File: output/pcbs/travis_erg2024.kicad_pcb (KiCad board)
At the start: 2 copper layers, 385.3 x 144.8 mm, 378 parts, among them SW1 SW_PUSH_6mm_H4.3mm

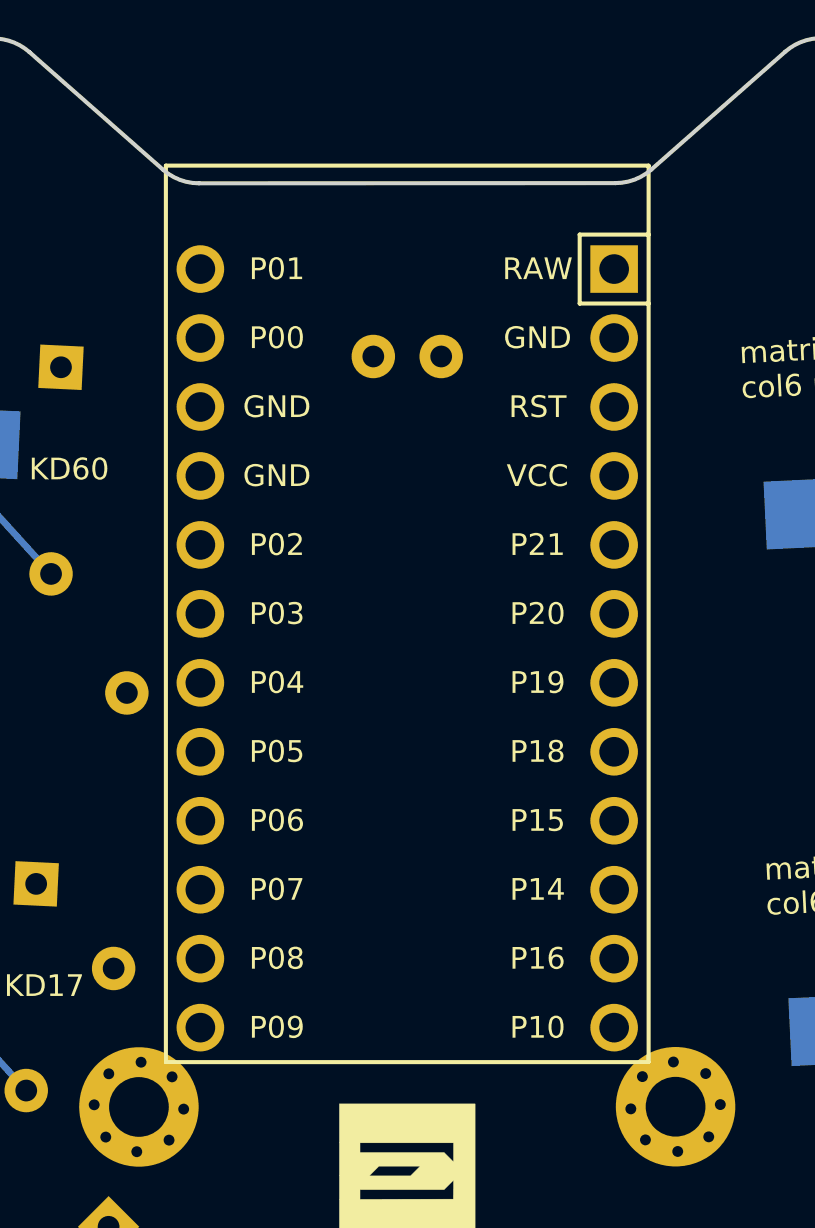
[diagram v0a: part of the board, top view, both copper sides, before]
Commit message: new mcu footprint, mux fixes
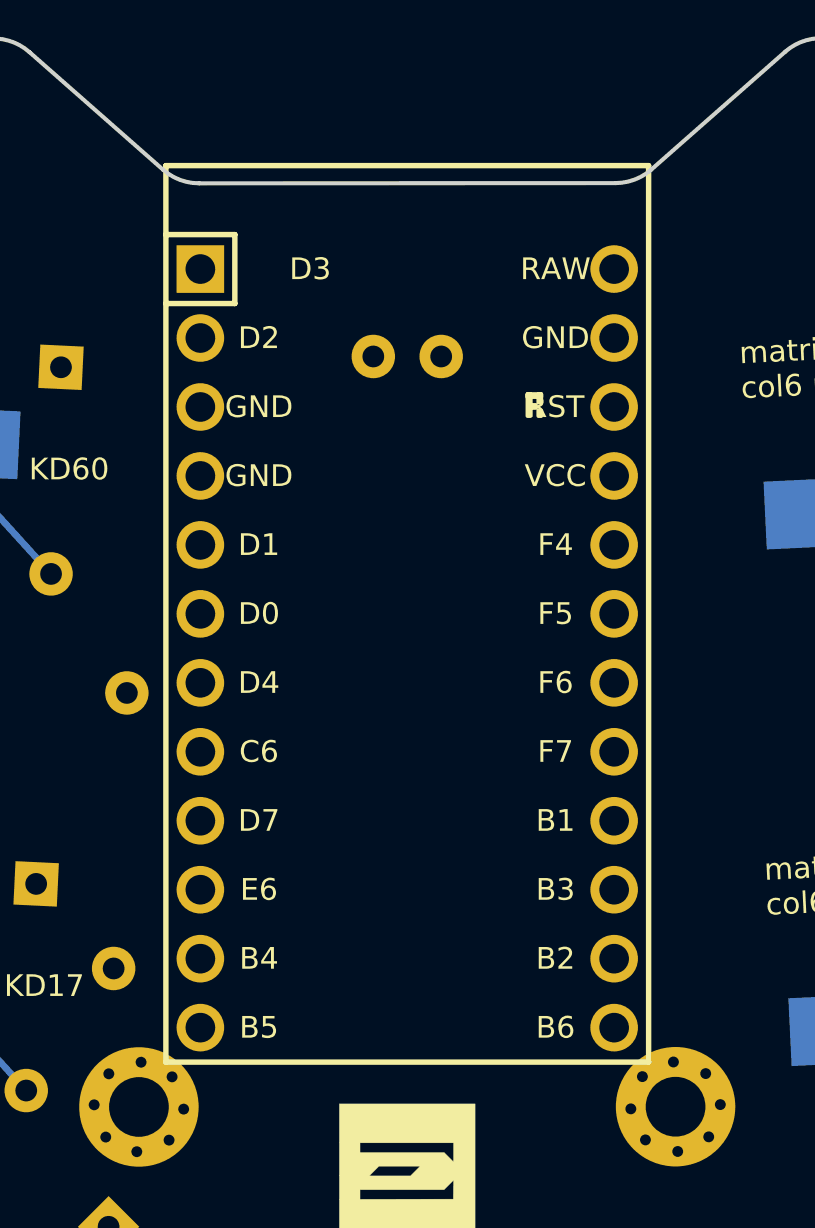
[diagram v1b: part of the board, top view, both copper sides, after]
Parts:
- DIP1, DIP2: value DIP-16_W7.62mm_Socket -> 74HC138N
- MCU1: value (none) -> Arduino_Pro_Micro; footprint ProMicro -> Arduino_Pro_Micro
- turned MCU1 to 0 degrees
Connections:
- DIP1 pad 10: col0 -> col2
- DIP1 pad 11: col1 -> col3
- DIP1 pad 12: col2 -> col4
- DIP1 pad 13: col3 -> col5
- DIP1 pad 14: col4 -> col6
- DIP1 pad 15: col5 -> col7
- DIP1 pad 7: row0 -> col0
- DIP1 pad 9: row1 -> col1
- MCU1 pad 1: RAW -> D3
- MCU1 pad 10: row5 -> scrA
- MCU1 pad 11: encA -> B4
- MCU1 pad 12: encC -> LED
- MCU1 pad 13: P1 -> encC
- MCU1 pad 14: P0 -> encA
- MCU1 pad 15: GND -> row5
- MCU1 pad 16: GND -> row4
- MCU1 pad 17: mux3 -> row3
- MCU1 pad 18: mux2 -> row2
- MCU1 pad 19: mux1 -> row1
- MCU1 pad 2: GND -> D2
- MCU1 pad 20: mux0 -> row0
- MCU1 pad 21: scrC -> VCC
- MCU1 pad 22: scrA -> RST
- MCU1 pad 23: P8 -> GND
- MCU1 pad 24: LED -> RAW
- MCU1 pad 3: RST -> GND
- MCU1 pad 4: VCC -> GND
- MCU1 pad 5: col7 -> mux3
- MCU1 pad 6: col6 -> mux2
- MCU1 pad 7: row2 -> mux1
- MCU1 pad 8: row3 -> mux0
- MCU1 pad 9: row4 -> scrC

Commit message: [200~evqwgd001~ footprint added
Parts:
- removed REF**: RollerEncoder_Panasonic_EVQWGD001, RollerEncoder_Panasonic_EVQWGD001
- added SCR1: RollerEncoder_Panasonic_EVQWGD001, travis:evqwgd001, F.Cu at (163.1, 142.0)
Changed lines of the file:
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@@
 (net 214 "RST")
 (net 215 "scr_to")
-(net 216 "undefined")
-(net 217 "enc_to")
+(net 216 "enc_to")
   (net_class Default "This is the default net class."
     (clearance 0.2)
@@
 (add_net "RST")
 (add_net "scr_to")
-(add_net "undefined")
 (add_net "enc_to")
   )
@@
         (effects (font (size 0.8 0.8) (thickness 0.15)))
     )
-    (fp_text user "D3" (at -3.571872 -13.97) (layer "F.SilkS")
+    (fp_text user "D3" (at -5.461 -13.97) (layer "F.SilkS")
         (effects (font (size 0.8 0.8) (thickness 0.15)))
     )
-    (fp_text user "D3" (at -3.571872 -13.97) (layer "B.SilkS")
+    (fp_text user "D3" (at -5.461 -13.97) (layer "B.SilkS")
         (effects (font (size 0.8 0.8) (thickness 0.15)) (justify mirror))
     )
@@
     )
   )
-        (module RollerEncoder_Panasonic_EVQWGD001 (layer F.Cu)
+        (module "travis:evqwgd001" (layer F.Cu)
         (at 163.14529764999997 141.96773245 0)
-        (fp_text reference REF** (at 0 0 0) (layer F.Fab) (effects (font (size 1 1) (thickness 0.15))))
-        (fp_text value RollerEncoder_Panasonic_EVQWGD001 (at -0.1 9 0) (layer F.Fab) (effects (font (size 1 1) (thickness 0.15))))
+        (attr through_hole)
+        (fp_text reference "SCR1" (at 0 0 0) (layer F.SilkS) hide
+            (effects (font (size 1 1) (thickness 0.15)))
+        )
+        (fp_text value "RollerEncoder_Panasonic_EVQWGD001" (at -0.1 9 0) (layer F.Fab) hide
+            (effects (font (size 0.8 0.8) (thickness 0.15)))
+        )
         (fp_line (start -8.4 -6.4) (end 8.4 -6.4) (layer Dwgs.User) (width 0.12))
         (fp_line (start 8.4 -6.4) (end 8.4 7.4) (layer Dwgs.User) (width 0.12))
@@
           (pad B thru_hole circle (at -5.625 -1.27 0) (size 1.6 1.6) (drill 0.9) (layers *.Cu *.Mask) (net 7 "GND"))
           (pad C thru_hole circle (at -5.625 1.27 0) (size 1.6 1.6) (drill 0.9) (layers *.Cu *.Mask) (net 208 "scrC"))
-          (pad D thru_hole circle (at -5.625 3.81 0) (size 1.6 1.6) (drill 0.9) (layers *.Cu *.Mask) (net 216 "undefined"))
+          (pad D thru_hole circle (at -5.625 3.81 0) (size 1.6 1.6) (drill 0.9) (layers *.Cu *.Mask) (net 0 ""))
           (pad "" np_thru_hole circle (at -5.625 6.3 0) (size 1.5 1.5) (drill 1.5) (layers *.Cu *.Mask))
-        )
+        (model "${TRAVIS_KICAD}/evqwgd001.step"
+    (offset (xyz 8.5 -7.4 -3.5))
+    (scale (xyz 1 1 1))
+    (rotate (xyz 0 0 -90))
+  )
+)
     (module "ScottoKeebs_Components:Diode_DO-35" (layer "B.Cu")
     (descr "Diode, DO-35_SOD27 series, Axial, Horizontal, pin pitch=7.62mm, , length*diameter=4*2mm^2, , http://www.diodes.com/_files/packages/DO-35.pdf")
@@
             (pad B thru_hole circle (at -7.62 2.46) (size 2 2) (drill 1) (layers *.Cu *.Mask) (net 7 "GND"))
             (pad 1 thru_hole circle (at 6.88 -2.54) (size 1.5 1.5) (drill 1) (layers *.Cu *.Mask) (net 38 "col4"))
-            (pad 2 thru_hole circle (at 6.88 2.46) (size 1.5 1.5) (drill 1) (layers *.Cu *.Mask) (net 217 "enc_to"))
+            (pad 2 thru_hole circle (at 6.88 2.46) (size 1.5 1.5) (drill 1) (layers *.Cu *.Mask) (net 216 "enc_to"))
             (pad "" thru_hole rect (at -0.12 -5.64 -90) (size 3.2 2) (drill oval 2.8 1.5) (layers *.Cu *.Mask))
             (pad "" thru_hole rect (at -0.12 5.56 -90)  (size 3.2 2) (drill oval 2.8 1.5) (layers *.Cu *.Mask))
@@
       (stroke (width 0.1) (type solid)) (layer "B.Fab") )
     (pad 1 thru_hole rect (at 0 0 45) (size 1.6 1.6) (drill 0.8) (layers "*.Cu" "*.Mask") (net 3 "row5"))
-    (pad 2 thru_hole oval (at 7.62 0 45) (size 1.6 1.6) (drill 0.8) (layers "*.Cu" "*.Mask") (net 217 "enc_to"))
+    (pad 2 thru_hole oval (at 7.62 0 45) (size 1.6 1.6) (drill 0.8) (layers "*.Cu" "*.Mask") (net 216 "enc_to"))
     (model "${SCOTTOKEEBS_KICAD}/3dmodels/ScottoKeebs_Components.3dshapes/Diode_DO-35.step"
       (offset (xyz 0 0 0))

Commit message: added ec11
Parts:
- ROT1: value (none) -> EC11; footprint rotary_encoder -> travis:ec11
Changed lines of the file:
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@@
     )
   )
-        (module rotary_encoder (layer F.Cu)
+        (module "travis:ec11" (layer F.Cu)
             (at 163.145297625 170.50982505000002 -90)
-            (fp_text reference "ROT1" (at 0 0.5) (layer F.SilkS)
-                hide (effects (font (size 1 1) (thickness 0.15))))
-            (fp_text value "" (at 0 8.89) (layer F.Fab)
-                (effects (font (size 1 1) (thickness 0.15))))
+            (fp_text reference "ROT1" (at 0 0.5 -90) (layer F.SilkS) hide
+                (effects (font (size 1 1) (thickness 0.15)))
+            )
+            (fp_text value "EC11" (at 0 8.89 -90) (layer F.Fab) hide
+                (effects (font (size 0.8 0.8) (thickness 0.15)))
+            )
             (fp_line (start -0.62 -0.04) (end 0.38 -0.04) (layer F.SilkS) (width 0.12))
             (fp_line (start -0.12 -0.54) (end -0.12 0.46) (layer F.SilkS) (width 0.12))
@@
             (pad "" thru_hole rect (at -0.12 -5.64 -90) (size 3.2 2) (drill oval 2.8 1.5) (layers *.Cu *.Mask))
             (pad "" thru_hole rect (at -0.12 5.56 -90)  (size 3.2 2) (drill oval 2.8 1.5) (layers *.Cu *.Mask))
+            (model "${TRAVIS_KICAD}/ec11.step"
+                (offset (xyz 0 0 0))
+                (scale (xyz 1 1 1))
+                (rotate (xyz 0 0 90))
+            )
         )
     (module "ScottoKeebs_Components:Diode_DO-35" (layer "B.Cu")

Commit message: wired v5
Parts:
- moved D1 5.30 mm to (157.1, 126.2), turned to -90 degrees
- moved D2 5.00 mm to (158.6, 185.0), turned to 90 degrees
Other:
- board text added: "2024.03.31"
- board text removed: "2024.03.25"
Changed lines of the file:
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@@
   (title_block
     (title travis_erg2024)
-    (rev 2024.03.25)
+    (rev 2024.03.31)
     (company "Travis Hardiman")
   )
@@
     (descr "Diode, DO-35_SOD27 series, Axial, Horizontal, pin pitch=7.62mm, , length*diameter=4*2mm^2, , http://www.diodes.com/_files/packages/DO-35.pdf")
     (tags "Diode DO-35_SOD27 series Axial Horizontal pin pitch 7.62mm  length 4mm diameter 2mm")
-    (at 152.14529764999997 127.96773245 -45)
-    (fp_text reference "D1" (at 3.81 -2.12 -45) (layer "B.SilkS") hide
+    (at 157.14529764999997 126.21773245 -90)
+    (fp_text reference "D1" (at 3.81 -2.12 -90) (layer "B.SilkS") hide
       (effects (font (size 1 1) (thickness 0.15)) (justify mirror))
     )
-    (fp_text value "1N4148" (at 3.81 0 -45) (layer "B.Fab")
+    (fp_text value "1N4148" (at 3.81 0 -90) (layer "B.Fab")
       (effects (font (size 0.8 0.8) (thickness 0.15)))
     )
@@
     (fp_line (start 7.62 0) (end 5.81 0)
       (stroke (width 0.1) (type solid)) (layer "B.Fab") )
-    (pad 1 thru_hole rect (at 0 0 -45) (size 1.6 1.6) (drill 0.8) (layers "*.Cu" "*.Mask") (net 122 "row0"))
-    (pad 2 thru_hole oval (at 7.62 0 -45) (size 1.6 1.6) (drill 0.8) (layers "*.Cu" "*.Mask") (net 215 "scr_to"))
+    (pad 1 thru_hole rect (at 0 0 -90) (size 1.6 1.6) (drill 0.8) (layers "*.Cu" "*.Mask") (net 122 "row0"))
+    (pad 2 thru_hole oval (at 7.62 0 -90) (size 1.6 1.6) (drill 0.8) (layers "*.Cu" "*.Mask") (net 215 "scr_to"))
     (model "${SCOTTOKEEBS_KICAD}/3dmodels/ScottoKeebs_Components.3dshapes/Diode_DO-35.step"
       (offset (xyz 0 0 0))
@@
     (descr "Diode, DO-35_SOD27 series, Axial, Horizontal, pin pitch=7.62mm, , length*diameter=4*2mm^2, , http://www.diodes.com/_files/packages/DO-35.pdf")
     (tags "Diode DO-35_SOD27 series Axial Horizontal pin pitch 7.62mm  length 4mm diameter 2mm")
-    (at 153.645297625 185.00982505000002 45)
-    (fp_text reference "D2" (at 3.81 -2.12 -45) (layer "B.SilkS") hide
+    (at 158.645297625 185.00982505000002 90)
+    (fp_text reference "D2" (at 3.81 -2.12 -90) (layer "B.SilkS") hide
       (effects (font (size 1 1) (thickness 0.15)) (justify mirror))
     )
-    (fp_text value "1N4148" (at 3.81 0 -45) (layer "B.Fab")
+    (fp_text value "1N4148" (at 3.81 0 -90) (layer "B.Fab")
       (effects (font (size 0.8 0.8) (thickness 0.15)))
     )
@@
     (fp_line (start 7.62 0) (end 5.81 0)
       (stroke (width 0.1) (type solid)) (layer "B.Fab") )
-    (pad 1 thru_hole rect (at 0 0 45) (size 1.6 1.6) (drill 0.8) (layers "*.Cu" "*.Mask") (net 3 "row5"))
-    (pad 2 thru_hole oval (at 7.62 0 45) (size 1.6 1.6) (drill 0.8) (layers "*.Cu" "*.Mask") (net 216 "enc_to"))
+    (pad 1 thru_hole rect (at 0 0 90) (size 1.6 1.6) (drill 0.8) (layers "*.Cu" "*.Mask") (net 3 "row5"))
+    (pad 2 thru_hole oval (at 7.62 0 90) (size 1.6 1.6) (drill 0.8) (layers "*.Cu" "*.Mask") (net 216 "enc_to"))
     (model "${SCOTTOKEEBS_KICAD}/3dmodels/ScottoKeebs_Components.3dshapes/Diode_DO-35.step"
       (offset (xyz 0 0 0))
@@
        (stroke (width 0) (type solid)) (fill solid) (layer F.Cu))
    )
-      (gr_text "2024.03.25" (at 163.14529770000001 200.22995045 0) (layer F.SilkS)
+      (gr_text "2024.03.31" (at 163.14529770000001 200.22995045 0) (layer F.SilkS)
         (effects (font (face "CaskaydiaMono NFP") (size 0.9 0.9) (thickness 0.15)))
       )

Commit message: minor value updates
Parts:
- C1: value C_Radial_D6.3mm_H11.0mm_P2.50mm -> 6.3V 1000uF
- C2, C3: value C_Disc_D3.8mm_W2.6mm_P2.50mm -> 104
- KLED1, KLED10, KLED11, KLED12, KLED13, KLED14, KLED15, KLED16, KLED17, KLED18, KLED19, KLED2, KLED20, KLED21, KLED22, KLED23, KLED24, KLED25, KLED26, KLED27, KLED28, KLED29, KLED3, KLED30, KLED31, KLED32, KLED33, KLED34, KLED35, KLED36, KLED37, KLED38, KLED39, KLED4, KLED40, KLED41, KLED42, KLED43, KLED44, KLED45, KLED46, KLED47, KLED48, KLED49, KLED5, KLED50, KLED51, KLED52, KLED53, KLED54, KLED55, KLED56, KLED57, KLED58, KLED59, KLED6, KLED60, KLED61, KLED62, KLED63, KLED64, KLED65, KLED66, KLED67, KLED68, KLED69, KLED7, KLED70, KLED71, KLED72, KLED73, KLED74, KLED75, KLED76, KLED77, KLED78, KLED79, KLED8, KLED80, KLED81, KLED82, KLED83, KLED84, KLED85, KLED86, KLED87, KLED88, KLED9: footprint travis:led_SK6812mini-e (per-key single-side) -> travis:led_SK6812mini-e
- MCU1: value Arduino_Pro_Micro -> Arduino Pro Micro
- R1: value R_Axial_DIN0207_L6.3mm_D2.5mm_P10.16mm_Horizontal -> 470R
- SCR1: value RollerEncoder_Panasonic_EVQWGD001 -> EVQWGD001
- SW1: value SW_PUSH_6mm_H4.3mm -> 6mm button
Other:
- board text added: "2024.04.01"
- board text removed: "2024.03.31"

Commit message: v6 of routing
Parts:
- C2, C3: footprint Capacitor_THT:C_Disc_D3.8mm_W2.6mm_P2.50mm -> Capacitor_THT:C_Disc_D4.7mm_W2.5mm_P5.00mm
- DIP1, DIP2: value 74HC138N -> SN74HC138N
- moved C3 1.27 mm to (267.5, 87.9)
- moved C2 1.27 mm to (63.3, 89.1)
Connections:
- DIP1 pad 10: col2 -> col5
- DIP1 pad 11: col3 -> col4
- DIP1 pad 12: col4 -> col3
- DIP1 pad 13: col5 -> col2
- DIP1 pad 14: col6 -> col1
- DIP1 pad 15: col7 -> col0
- DIP1 pad 7: col0 -> col7
- DIP1 pad 9: col1 -> col6
- DIP2 pad 10: col10 -> col13
- DIP2 pad 11: col11 -> col12
- DIP2 pad 12: col12 -> col11
- DIP2 pad 13: col13 -> col10
- DIP2 pad 14: col14 -> col9
- DIP2 pad 15: col15 -> col8
- DIP2 pad 7: col8 -> col15
- DIP2 pad 9: col9 -> col14
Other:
- board text added: "2024.04.05"
- board text removed: "2024.04.01"

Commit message: add row2col option and use that
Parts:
- removed KLED1, KLED10, KLED11, KLED12, KLED13, KLED14, KLED15, KLED16, KLED17, KLED18, KLED19, KLED2, KLED20, KLED21, KLED22, KLED23, KLED24, KLED25, KLED26, KLED27, KLED28, KLED29, KLED3, KLED30, KLED31, KLED32, KLED33, KLED34, KLED35, KLED36, KLED37, KLED38, KLED39, KLED4, KLED40, KLED41, KLED42, KLED43, KLED44, KLED45, KLED46, KLED47, KLED48, KLED49, KLED5, KLED50, KLED51, KLED52, KLED53, KLED54, KLED55, KLED56, KLED57, KLED58, KLED59, KLED6, KLED60, KLED61, KLED62, KLED63, KLED64, KLED65, KLED66, KLED67, KLED68, KLED69, KLED7, KLED70, KLED71, KLED72, KLED73, KLED74, KLED75, KLED76, KLED77, KLED78, KLED79, KLED8, KLED80, KLED81, KLED82, KLED83, KLED84, KLED85, KLED86, KLED87, KLED88, KLED9: SK6812mini-e, travis:led_SK6812mini-e
- added LED_0-row0-col5: SK6812mini-e, travis:led_SK6812mini-e, B.Cu at (141.3, 108.9)
- added LED_1-row0-col4: SK6812mini-e, travis:led_SK6812mini-e, B.Cu at (121.8, 107.8)
- added LED_10-row1-col5: SK6812mini-e, travis:led_SK6812mini-e, B.Cu at (140.3, 127.9)
- added LED_11-row2-col5: SK6812mini-e, travis:led_SK6812mini-e, B.Cu at (139.4, 146.9)
- added LED_12-row2-col4: SK6812mini-e, travis:led_SK6812mini-e, B.Cu at (120.2, 145.8)
- added LED_13-row2-col3: SK6812mini-e, travis:led_SK6812mini-e, B.Cu at (100.2, 144.3)
- added LED_14-row2-col2: SK6812mini-e, travis:led_SK6812mini-e, B.Cu at (80.3, 145.1)
- added LED_15-row2-col1: SK6812mini-e, travis:led_SK6812mini-e, B.Cu at (60.3, 147.3)
- added LED_16-row2-col0: SK6812mini-e, travis:led_SK6812mini-e, B.Cu at (36.0, 147.5)
- added LED_17-row3-col0: SK6812mini-e, travis:led_SK6812mini-e, B.Cu at (36.2, 166.6)
- added LED_18-row3-col1: SK6812mini-e, travis:led_SK6812mini-e, B.Cu at (60.5, 166.3)
- added LED_19-row3-col2: SK6812mini-e, travis:led_SK6812mini-e, B.Cu at (80.1, 164.2)
- added LED_2-row0-col3: SK6812mini-e, travis:led_SK6812mini-e, B.Cu at (101.2, 106.2)
- added LED_20-row3-col3: SK6812mini-e, travis:led_SK6812mini-e, B.Cu at (99.8, 163.3)
- added LED_21-row3-col4: SK6812mini-e, travis:led_SK6812mini-e, B.Cu at (119.3, 164.9)
- added LED_22-row3-col5: SK6812mini-e, travis:led_SK6812mini-e, B.Cu at (138.5, 166.0)
- added LED_23-row4-col5: SK6812mini-e, travis:led_SK6812mini-e, B.Cu at (137.6, 185.0)
- added LED_24-row4-col4: SK6812mini-e, travis:led_SK6812mini-e, B.Cu at (118.5, 183.9)
- added LED_25-row4-col3: SK6812mini-e, travis:led_SK6812mini-e, B.Cu at (99.3, 182.4)
- added LED_26-row4-col2: SK6812mini-e, travis:led_SK6812mini-e, B.Cu at (79.9, 183.2)
- added LED_27-row4-col1: SK6812mini-e, travis:led_SK6812mini-e, B.Cu at (60.7, 185.4)
- added LED_28-row4-col0: SK6812mini-e, travis:led_SK6812mini-e, B.Cu at (36.4, 185.6)
- added LED_29-row5-col0: SK6812mini-e, travis:led_SK6812mini-e, B.Cu at (41.8, 204.6)
- added LED_3-row0-col2: SK6812mini-e, travis:led_SK6812mini-e, B.Cu at (80.6, 107.0)
- added LED_30-row5-col1: SK6812mini-e, travis:led_SK6812mini-e, B.Cu at (60.8, 204.4)
- added LED_31-row5-col2: SK6812mini-e, travis:led_SK6812mini-e, B.Cu at (79.8, 202.3)
- added LED_32-row5-col3: SK6812mini-e, travis:led_SK6812mini-e, B.Cu at (98.8, 201.4)
- added LED_33-row5-col5: SK6812mini-e, travis:led_SK6812mini-e, B.Cu at (135.2, 203.9)
- added LED_34-row5-col6: SK6812mini-e, travis:led_SK6812mini-e, B.Cu at (191.1, 203.9)
- added LED_35-row5-col8: SK6812mini-e, travis:led_SK6812mini-e, B.Cu at (227.5, 200.9)
- added LED_36-row5-col9: SK6812mini-e, travis:led_SK6812mini-e, B.Cu at (246.5, 201.3)
- added LED_37-row5-col10: SK6812mini-e, travis:led_SK6812mini-e, B.Cu at (265.5, 203.1)
- added LED_38-row5-col11: SK6812mini-e, travis:led_SK6812mini-e, B.Cu at (284.5, 203.2)
- added LED_39-row5-col14: SK6812mini-e, travis:led_SK6812mini-e, B.Cu at (326.7, 198.8)
- added LED_4-row0-col0: SK6812mini-e, travis:led_SK6812mini-e, B.Cu at (41.0, 109.4)
- added LED_40-row5-col15: SK6812mini-e, travis:led_SK6812mini-e, B.Cu at (340.8, 211.6)
- added LED_41-row4-col15: SK6812mini-e, travis:led_SK6812mini-e, B.Cu at (353.6, 197.5)
- added LED_42-row4-col14: SK6812mini-e, travis:led_SK6812mini-e, B.Cu at (339.5, 184.7)
- added LED_43-row4-col11: SK6812mini-e, travis:led_SK6812mini-e, B.Cu at (290.0, 184.2)
- added LED_44-row4-col10: SK6812mini-e, travis:led_SK6812mini-e, B.Cu at (265.6, 184.0)
- added LED_45-row4-col9: SK6812mini-e, travis:led_SK6812mini-e, B.Cu at (246.3, 182.3)
- added LED_46-row4-col8: SK6812mini-e, travis:led_SK6812mini-e, B.Cu at (226.9, 181.9)
- added LED_47-row4-col7: SK6812mini-e, travis:led_SK6812mini-e, B.Cu at (207.7, 183.8)
- added LED_48-row4-col6: SK6812mini-e, travis:led_SK6812mini-e, B.Cu at (188.7, 185.0)
- added LED_49-row3-col6: SK6812mini-e, travis:led_SK6812mini-e, B.Cu at (187.8, 165.9)
- added LED_5-row1-col0: SK6812mini-e, travis:led_SK6812mini-e, B.Cu at (41.1, 128.4)
- added LED_50-row3-col7: SK6812mini-e, travis:led_SK6812mini-e, B.Cu at (206.8, 164.8)
- added LED_51-row3-col8: SK6812mini-e, travis:led_SK6812mini-e, B.Cu at (226.4, 162.8)
- added LED_52-row3-col9: SK6812mini-e, travis:led_SK6812mini-e, B.Cu at (246.0, 163.3)
- added LED_53-row3-col10: SK6812mini-e, travis:led_SK6812mini-e, B.Cu at (265.7, 165.0)
- added LED_54-row3-col11: SK6812mini-e, travis:led_SK6812mini-e, B.Cu at (284.7, 165.1)
- added LED_55-row3-col12: SK6812mini-e, travis:led_SK6812mini-e, B.Cu at (309.1, 165.2)
- added LED_56-row3-col14: SK6812mini-e, travis:led_SK6812mini-e, B.Cu at (355.5, 167.1)
- added LED_57-row3-col15: SK6812mini-e, travis:led_SK6812mini-e, B.Cu at (369.6, 179.9)
- added LED_58-row2-col15: SK6812mini-e, travis:led_SK6812mini-e, B.Cu at (382.4, 165.8)
- added LED_59-row2-col14: SK6812mini-e, travis:led_SK6812mini-e, B.Cu at (368.3, 153.0)
- added LED_6-row1-col1: SK6812mini-e, travis:led_SK6812mini-e, B.Cu at (60.2, 128.2)
- added LED_60-row2-col13: SK6812mini-e, travis:led_SK6812mini-e, B.Cu at (322.9, 146.2)
- added LED_61-row2-col12: SK6812mini-e, travis:led_SK6812mini-e, B.Cu at (303.8, 146.1)
- added LED_62-row2-col11: SK6812mini-e, travis:led_SK6812mini-e, B.Cu at (284.8, 146.0)
- added LED_63-row2-col10: SK6812mini-e, travis:led_SK6812mini-e, B.Cu at (265.7, 145.9)
- added LED_64-row2-col9: SK6812mini-e, travis:led_SK6812mini-e, B.Cu at (245.8, 144.2)
- added LED_65-row2-col8: SK6812mini-e, travis:led_SK6812mini-e, B.Cu at (225.8, 143.8)
- added LED_66-row2-col7: SK6812mini-e, travis:led_SK6812mini-e, B.Cu at (205.9, 145.8)
- added LED_67-row2-col6: SK6812mini-e, travis:led_SK6812mini-e, B.Cu at (186.9, 146.9)
- added LED_68-row1-col6: SK6812mini-e, travis:led_SK6812mini-e, B.Cu at (186.0, 127.9)
- added LED_69-row1-col7: SK6812mini-e, travis:led_SK6812mini-e, B.Cu at (205.0, 126.7)
- added LED_7-row1-col2: SK6812mini-e, travis:led_SK6812mini-e, B.Cu at (80.4, 126.1)
- added LED_70-row1-col8: SK6812mini-e, travis:led_SK6812mini-e, B.Cu at (225.2, 124.8)
- added LED_71-row1-col9: SK6812mini-e, travis:led_SK6812mini-e, B.Cu at (245.5, 125.2)
- added LED_72-row1-col10: SK6812mini-e, travis:led_SK6812mini-e, B.Cu at (265.8, 126.9)
- added LED_73-row1-col11: SK6812mini-e, travis:led_SK6812mini-e, B.Cu at (284.9, 127.0)
- added LED_74-row1-col12: SK6812mini-e, travis:led_SK6812mini-e, B.Cu at (303.9, 127.1)
- added LED_75-row1-col13: SK6812mini-e, travis:led_SK6812mini-e, B.Cu at (328.3, 127.2)
- added LED_76-row1-col14: SK6812mini-e, travis:led_SK6812mini-e, B.Cu at (370.6, 127.4)
- added LED_77-row1-col15: SK6812mini-e, travis:led_SK6812mini-e, B.Cu at (389.6, 127.4)
- added LED_78-row0-col15: SK6812mini-e, travis:led_SK6812mini-e, B.Cu at (389.7, 108.4)
- added LED_79-row0-col14: SK6812mini-e, travis:led_SK6812mini-e, B.Cu at (370.7, 108.3)
- added LED_8-row1-col3: SK6812mini-e, travis:led_SK6812mini-e, B.Cu at (100.7, 125.3)
- added LED_80-row3-col13: SK6812mini-e, travis:led_SK6812mini-e, B.Cu at (342.1, 108.2)
- added LED_81-row0-col13: SK6812mini-e, travis:led_SK6812mini-e, B.Cu at (323.1, 108.1)
- added LED_82-row0-col12: SK6812mini-e, travis:led_SK6812mini-e, B.Cu at (304.0, 108.0)
- added LED_83-row0-col11: SK6812mini-e, travis:led_SK6812mini-e, B.Cu at (285.0, 107.9)
- added LED_84-row0-col9: SK6812mini-e, travis:led_SK6812mini-e, B.Cu at (245.3, 106.1)
- added LED_85-row0-col8: SK6812mini-e, travis:led_SK6812mini-e, B.Cu at (224.6, 105.7)
- added LED_86-row0-col7: SK6812mini-e, travis:led_SK6812mini-e, B.Cu at (204.1, 107.7)
- added LED_87-row0-col6: SK6812mini-e, travis:led_SK6812mini-e, B.Cu at (185.0, 108.9)
- added LED_9-row1-col4: SK6812mini-e, travis:led_SK6812mini-e, B.Cu at (121.0, 126.8)
- moved KD54 8.43 mm to (109.9, 101.9), turned to 88.5 degrees
- moved KD79 8.43 mm to (312.6, 103.5), turned to 89.75 degrees
- moved KD74 8.43 mm to (274.3, 141.4), turned to 89.75 degrees
- moved KD34 8.43 mm to (293.4, 122.5), turned to 89.75 degrees
- moved KD39 8.43 mm to (356.0, 188.1), turned to 137.75 degrees
- moved KD41 8.43 mm to (384.8, 156.4), turned to 137.75 degrees
- moved KD24 8.43 mm to (234.7, 158.0), turned to 91.75 degrees
- moved KD25 8.43 mm to (233.6, 120.0), turned to 91.75 degrees
- moved KD68 8.43 mm to (234.2, 139.0), turned to 91.75 degrees
- moved KD69 8.43 mm to (233.0, 100.9), turned to 91.75 degrees
- moved KD55 8.43 mm to (127.2, 179.7), turned to 87.5 degrees
- moved KD56 8.43 mm to (128.9, 141.7), turned to 87.5 degrees
- moved KD57 8.43 mm to (130.6, 103.6), turned to 87.5 degrees
- moved KD13 8.43 mm to (128.1, 160.7), turned to 87.5 degrees
- moved KD14 8.43 mm to (129.7, 122.6), turned to 87.5 degrees
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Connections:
- D1 pad 1: row0 -> scr_to
- D1 pad 2: scr_to -> row0
- D2 pad 1: row5 -> enc_to
- D2 pad 2: enc_to -> row5
- KD1 pad 1: row5 -> matrixl_outer_mod
- KD1 pad 2: matrixl_outer_mod -> row5
- KD10 pad 1: row5 -> matrixl_middle_mod
- KD10 pad 2: matrixl_middle_mod -> row5
- KD11 pad 1: row3 -> matrixl_middle_home
- KD11 pad 2: matrixl_middle_home -> row3
- KD12 pad 1: row1 -> matrixl_middle_num
- KD12 pad 2: matrixl_middle_num -> row1
- KD13 pad 1: row3 -> matrixl_index_home
- KD13 pad 2: matrixl_index_home -> row3
- KD14 pad 1: row1 -> matrixl_index_num
- KD14 pad 2: matrixl_index_num -> row1
- KD15 pad 1: row5 -> matrixl_inner_mod
- KD15 pad 2: matrixl_inner_mod -> row5
- KD16 pad 1: row3 -> matrixl_inner_home
- KD16 pad 2: matrixl_inner_home -> row3
- KD17 pad 1: row1 -> matrixl_inner_num
- KD17 pad 2: matrixl_inner_num -> row1
- KD18 pad 1: row5 -> matrixr_inner_mod
- KD18 pad 2: matrixr_inner_mod -> row5
- KD19 pad 1: row3 -> matrixr_inner_home
- KD19 pad 2: matrixr_inner_home -> row3
- KD2 pad 1: row3 -> matrixl_outer_home
- KD2 pad 2: matrixl_outer_home -> row3
- KD20 pad 1: row1 -> matrixr_inner_num
- KD20 pad 2: matrixr_inner_num -> row1
- KD21 pad 1: row3 -> matrixr_index_home
- KD21 pad 2: matrixr_index_home -> row3
- KD22 pad 1: row1 -> matrixr_index_num
- KD22 pad 2: matrixr_index_num -> row1
- KD23 pad 1: row5 -> matrixr_middle_mod
- KD23 pad 2: matrixr_middle_mod -> row5
- KD24 pad 1: row3 -> matrixr_middle_home
- KD24 pad 2: matrixr_middle_home -> row3
- KD25 pad 1: row1 -> matrixr_middle_num
- KD25 pad 2: matrixr_middle_num -> row1
- KD26 pad 1: row5 -> matrixr_ring_mod
- KD26 pad 2: matrixr_ring_mod -> row5
- KD27 pad 1: row3 -> matrixr_ring_home
- KD27 pad 2: matrixr_ring_home -> row3
- KD28 pad 1: row1 -> matrixr_ring_num
- KD28 pad 2: matrixr_ring_num -> row1
- KD29 pad 1: row5 -> matrixr_pinky_mod
- KD29 pad 2: matrixr_pinky_mod -> row5
- KD3 pad 1: row1 -> matrixl_outer_num
- KD3 pad 2: matrixl_outer_num -> row1
- KD30 pad 1: row3 -> matrixr_pinky_home
- KD30 pad 2: matrixr_pinky_home -> row3
- KD31 pad 1: row1 -> matrixr_pinky_num
- KD31 pad 2: matrixr_pinky_num -> row1
- KD32 pad 1: row5 -> matrixr_outer_mod
- KD32 pad 2: matrixr_outer_mod -> row5
- KD33 pad 1: row3 -> matrixr_outer_home
- KD33 pad 2: matrixr_outer_home -> row3
- KD34 pad 1: row1 -> matrixr_outer_num
- KD34 pad 2: matrixr_outer_num -> row1
- KD35 pad 1: row3 -> matrixr_outer2_home
- KD35 pad 2: matrixr_outer2_home -> row3
- KD36 pad 1: row1 -> matrixr_outer2_num
- KD36 pad 2: matrixr_outer2_num -> row1
- KD37 pad 1: row1 -> matrixr_outer3_num
- KD37 pad 2: matrixr_outer3_num -> row1
- KD38 pad 1: row5 -> arrows_left_bottom
- KD38 pad 2: arrows_left_bottom -> row5
- KD39 pad 1: row4 -> arrows_right_bottom
- KD39 pad 2: arrows_right_bottom -> row4
- KD4 pad 1: row5 -> matrixl_pinky_mod
- KD4 pad 2: matrixl_pinky_mod -> row5
- KD40 pad 1: row3 -> pages_left_bottom
- KD40 pad 2: pages_left_bottom -> row3
- KD41 pad 1: row2 -> pages_right_bottom
- KD41 pad 2: pages_right_bottom -> row2
- KD42 pad 1: row1 -> special_left_bottom
- KD42 pad 2: special_left_bottom -> row1
- KD43 pad 1: row1 -> special_right_bottom
- KD43 pad 2: special_right_bottom -> row1
- KD44 pad 1: row4 -> matrixl_outer_bottom
- KD44 pad 2: matrixl_outer_bottom -> row4
- KD45 pad 1: row2 -> matrixl_outer_top
- KD45 pad 2: matrixl_outer_top -> row2
- KD46 pad 1: row0 -> matrixl_outer_func
- KD46 pad 2: matrixl_outer_func -> row0
- KD47 pad 1: row4 -> matrixl_pinky_bottom
- KD47 pad 2: matrixl_pinky_bottom -> row4
- KD48 pad 1: row2 -> matrixl_pinky_top
- KD48 pad 2: matrixl_pinky_top -> row2
- KD49 pad 1: row4 -> matrixl_ring_bottom
- KD49 pad 2: matrixl_ring_bottom -> row4
- KD5 pad 1: row3 -> matrixl_pinky_home
- KD5 pad 2: matrixl_pinky_home -> row3
- KD50 pad 1: row2 -> matrixl_ring_top
- KD50 pad 2: matrixl_ring_top -> row2
- KD51 pad 1: row0 -> matrixl_ring_func
- KD51 pad 2: matrixl_ring_func -> row0
- KD52 pad 1: row4 -> matrixl_middle_bottom
- KD52 pad 2: matrixl_middle_bottom -> row4
- KD53 pad 1: row2 -> matrixl_middle_top
- KD53 pad 2: matrixl_middle_top -> row2
- KD54 pad 1: row0 -> matrixl_middle_func
- KD54 pad 2: matrixl_middle_func -> row0
- KD55 pad 1: row4 -> matrixl_index_bottom
- KD55 pad 2: matrixl_index_bottom -> row4
- KD56 pad 1: row2 -> matrixl_index_top
- KD56 pad 2: matrixl_index_top -> row2
- KD57 pad 1: row0 -> matrixl_index_func
- KD57 pad 2: matrixl_index_func -> row0
- KD58 pad 1: row4 -> matrixl_inner_bottom
- KD58 pad 2: matrixl_inner_bottom -> row4
- KD59 pad 1: row2 -> matrixl_inner_top
- KD59 pad 2: matrixl_inner_top -> row2
- KD6 pad 1: row1 -> matrixl_pinky_num
- KD6 pad 2: matrixl_pinky_num -> row1
- KD60 pad 1: row0 -> matrixl_inner_func
- KD60 pad 2: matrixl_inner_func -> row0
- KD61 pad 1: row4 -> matrixr_inner_bottom
- KD61 pad 2: matrixr_inner_bottom -> row4
- KD62 pad 1: row2 -> matrixr_inner_top
- KD62 pad 2: matrixr_inner_top -> row2
- KD63 pad 1: row0 -> matrixr_inner_func
- KD63 pad 2: matrixr_inner_func -> row0
- KD64 pad 1: row4 -> matrixr_index_bottom
- KD64 pad 2: matrixr_index_bottom -> row4
- KD65 pad 1: row2 -> matrixr_index_top
- KD65 pad 2: matrixr_index_top -> row2
- KD66 pad 1: row0 -> matrixr_index_func
- KD66 pad 2: matrixr_index_func -> row0
- KD67 pad 1: row4 -> matrixr_middle_bottom
- KD67 pad 2: matrixr_middle_bottom -> row4
- KD68 pad 1: row2 -> matrixr_middle_top
- KD68 pad 2: matrixr_middle_top -> row2
- KD69 pad 1: row0 -> matrixr_middle_func
- KD69 pad 2: matrixr_middle_func -> row0
- KD7 pad 1: row5 -> matrixl_ring_mod
- KD7 pad 2: matrixl_ring_mod -> row5
- KD70 pad 1: row4 -> matrixr_ring_bottom
- KD70 pad 2: matrixr_ring_bottom -> row4
- KD71 pad 1: row2 -> matrixr_ring_top
- KD71 pad 2: matrixr_ring_top -> row2
- KD72 pad 1: row0 -> matrixr_ring_func
- KD72 pad 2: matrixr_ring_func -> row0
- KD73 pad 1: row4 -> matrixr_pinky_bottom
- KD73 pad 2: matrixr_pinky_bottom -> row4
- KD74 pad 1: row2 -> matrixr_pinky_top
- KD74 pad 2: matrixr_pinky_top -> row2
- KD75 pad 1: row4 -> matrixr_outer_bottom
- KD75 pad 2: matrixr_outer_bottom -> row4
- KD76 pad 1: row2 -> matrixr_outer_top
- KD76 pad 2: matrixr_outer_top -> row2
- KD77 pad 1: row0 -> matrixr_outer_func
- KD77 pad 2: matrixr_outer_func -> row0
- KD78 pad 1: row2 -> matrixr_outer2_top
- KD78 pad 2: matrixr_outer2_top -> row2
- KD79 pad 1: row0 -> matrixr_outer2_func
- KD79 pad 2: matrixr_outer2_func -> row0
- KD8 pad 1: row3 -> matrixl_ring_home
- KD8 pad 2: matrixl_ring_home -> row3
- KD80 pad 1: row2 -> matrixr_outer3_top
- KD80 pad 2: matrixr_outer3_top -> row2
- KD81 pad 1: row0 -> matrixr_outer3_func
- KD81 pad 2: matrixr_outer3_func -> row0
- KD82 pad 1: row3 -> matrixr_outer4_func
- KD82 pad 2: matrixr_outer4_func -> row3
- KD83 pad 1: row5 -> arrows_left_top
- KD83 pad 2: arrows_left_top -> row5
- KD84 pad 1: row4 -> arrows_right_top
- KD84 pad 2: arrows_right_top -> row4
- KD85 pad 1: row3 -> pages_left_top
- KD85 pad 2: pages_left_top -> row3
- KD86 pad 1: row2 -> pages_right_top
- KD86 pad 2: pages_right_top -> row2
- KD87 pad 1: row0 -> special_left_top
- KD87 pad 2: special_left_top -> row0
- KD88 pad 1: row0 -> special_right_top
- KD88 pad 2: special_right_top -> row0
- KD9 pad 1: row1 -> matrixl_ring_num
- KD9 pad 2: matrixl_ring_num -> row1

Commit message: v update
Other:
- board text added: "2024.04.30"
- board text removed: "2024.04.05"
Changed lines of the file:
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@@
   (title_block
     (title travis_erg2024)
-    (rev 2024.04.05)
+    (rev 2024.04.30)
     (company "Travis Hardiman")
   )
@@
       (stroke (width 0) (type solid)) (fill solid) (layer "F.SilkS"))
    )
-      (gr_text "2024.04.05" (at 163.14529770000001 200.22995045 0) (layer F.SilkS)
+      (gr_text "2024.04.30" (at 163.14529770000001 200.22995045 0) (layer F.SilkS)
         (effects (font (size 0.9 0.9) (thickness 0.15)))
       )
